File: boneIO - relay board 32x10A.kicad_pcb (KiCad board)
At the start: 2 copper layers, 197 x 102 mm, 116 parts, among them J1 Screw_Terminal_01x03, J10 Screw_Terminal_01x03, J11 Screw_Terminal_01x03, J12 Conn_02x04_Odd_Even, J13 Screw_Terminal_01x03, J14 Screw_Terminal_01x03, J15 Screw_Terminal_01x03, J16 Screw_Terminal_01x03, J17 Screw_Terminal_01x03, J2 Screw_Terminal_01x03, J3 Screw_Terminal_01x03, J4 Screw_Terminal_01x03, J5 Screw_Terminal_01x03, J6 Screw_Terminal_01x03, J7 Screw_Terminal_01x03, J8 Screw_Terminal_01x03, J9 Screw_Terminal_01x03, K1 HF32F/024-ZS3, K10 HF32F/024-ZS3, K11 HF32F/024-ZS3, K12 HF32F/024-ZS3, K13 HF32F/024-ZS3, K14 HF32F/024-ZS3, K15 HF32F/024-ZS3, K16 HF32F/024-ZS3, K17 HF32F/024-ZS3, K18 HF32F/024-ZS3, K19 HF32F/024-ZS3, K2 HF32F/024-ZS3, K20 HF32F/024-ZS3, K21 HF32F/024-ZS3, K22 HF32F/024-ZS3, K23 HF32F/024-ZS3, K24 HF32F/024-ZS3, K25 HF32F/024-ZS3, K26 HF32F/024-ZS3, K27 HF32F/024-ZS3, K28 HF32F/024-ZS3, K29 HF32F/024-ZS3, K3 HF32F/024-ZS3, K30 HF32F/024-ZS3, K31 HF32F/024-ZS3, K32 HF32F/024-ZS3, K4 HF32F/024-ZS3, K5 HF32F/024-ZS3, K6 HF32F/024-ZS3, K7 HF32F/024-ZS3, K8 HF32F/024-ZS3, K9 HF32F/024-ZS3, SW1 SW_DIP_x03, SW2 SW_DIP_x03, SW3 SW_DIP_x03, U1 PCF8575, U2 ULN2803A, U21 MCP9808_SO8, U22 LM75_MSOP, U3 ULN2803A, U4 PCF8575, U5 ULN2803A, U6 ULN2803A

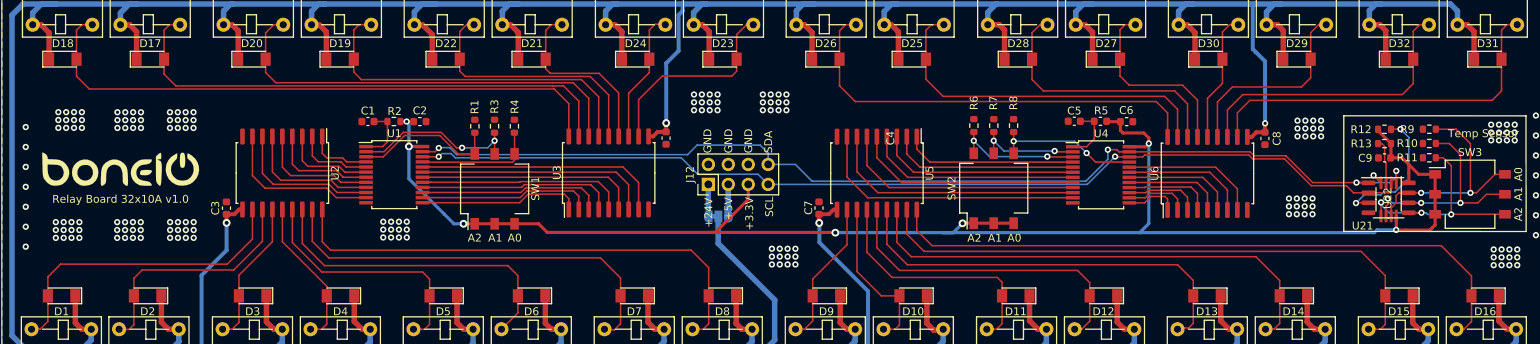
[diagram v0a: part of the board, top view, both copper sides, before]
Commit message: relay board 32x10A v0.1
Dodanie PCF8575
Dodanie MCP23017
Dodanie diody LL4148
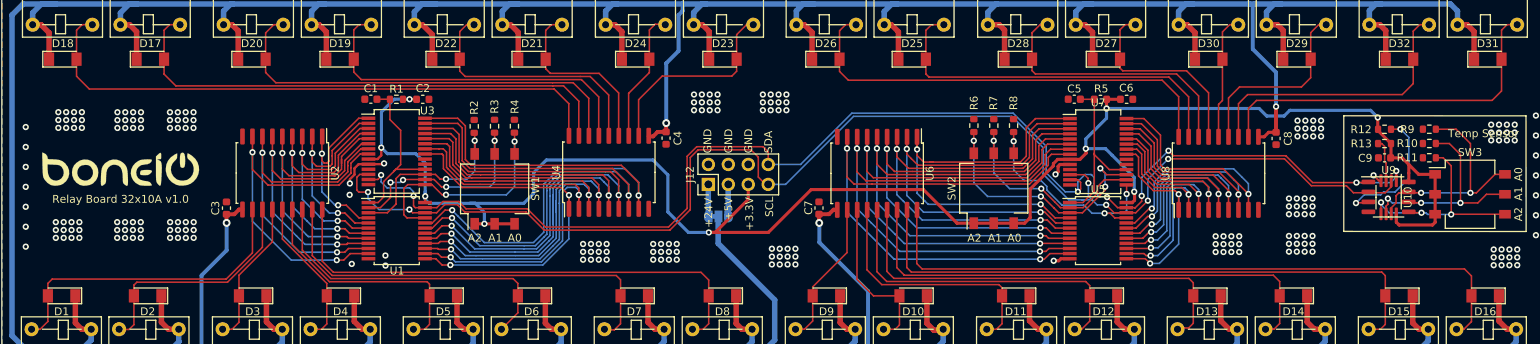
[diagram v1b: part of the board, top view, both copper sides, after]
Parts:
- removed U21: MCP9808_SO8, Package_SO:SO-8_3.9x4.9mm_P1.27mm
- removed U22: LM75_MSOP, Package_SO:MSOP-8_3x3mm_P0.65mm
- added U10: LM75_MSOP, Package_SO:MSOP-8_3x3mm_P0.65mm, F.Cu at (464.8, 314.4)
- added U7: MCP23017_SS, Package_SO:SSOP-28_5.3x10.2mm_P0.65mm, F.Cu at (427.8, 308.6)
- added U8: ULN2803A, Package_SO:SOIC-18W_7.5x11.6mm_P1.27mm, F.Cu at (443.1, 311.3)
- added U9: MCP9808_SO8, Package_SO:SO-8_3.9x4.9mm_P1.27mm, F.Cu at (464.8, 314.3)
- R1: value 10k -> 4.7k
- R2: value 4.7k -> 10k
- U3: value ULN2803A -> MCP23017_SS; footprint Package_SO:SOIC-18W_7.5x11.6mm_P1.27mm -> Package_SO:SSOP-28_5.3x10.2mm_P0.65mm
- U4: value PCF8575 -> ULN2803A; footprint Package_SO:SSOP-24_5.3x8.2mm_P0.65mm -> Package_SO:SOIC-18W_7.5x11.6mm_P1.27mm
- U5: value ULN2803A -> PCF8575; footprint Package_SO:SOIC-18W_7.5x11.6mm_P1.27mm -> Package_SO:SSOP-24_5.3x8.2mm_P0.65mm
- moved U4 62.7 mm to (365.5, 311.2), turned to 90 degrees
- moved U6 42.1 mm to (399.6, 311.3), turned to -90 degrees
- moved U5 29.1 mm to (427.8, 318.6), turned to 0 degrees
- moved U3 27.1 mm to (338.4, 308.5), turned to 0 degrees
- moved R1 10.6 mm to (338.4, 301.9), turned to 180 degrees
- moved R2 10.2 mm to (348.3, 305.3), turned to 90 degrees
- moved U1 7.14 mm to (338.4, 318.6)
- moved C2 2.86 mm to (341.8, 301.9)
- moved C1 2.86 mm to (335.2, 301.9)
- moved C6 2.85 mm to (431.4, 301.9)
- moved C5 2.81 mm to (424.8, 301.9)
- moved R5 2.80 mm to (428.1, 301.9)
- moved C8 1.42 mm to (450.5, 306.9)
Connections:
- C1 pad 1: Net-(C1-Pad1) -> INT_01
- C5 pad 1: Net-(C5-Pad1) -> INT_02
- R1 pad 1: Net-(R1-Pad1) -> +3V3
- R1 pad 2: GND -> INT_01
- R2 pad 1: +3V3 -> A2_1
- R2 pad 2: Net-(C1-Pad1) -> GND
- R3 pad 1: Net-(R3-Pad1) -> A1_1
- R4 pad 1: Net-(R4-Pad1) -> A0_1
- R5 pad 2: Net-(C5-Pad1) -> INT_02
- R6 pad 1: Net-(R6-Pad1) -> A2_2
- R7 pad 1: Net-(R7-Pad1) -> A1_2
- R8 pad 1: Net-(R8-Pad1) -> A0_2
- SW1 pad 4: Net-(R4-Pad1) -> A0_1
- SW1 pad 5: Net-(R3-Pad1) -> A1_1
- SW1 pad 6: Net-(R1-Pad1) -> A2_1
- SW2 pad 4: Net-(R8-Pad1) -> A0_2
- SW2 pad 5: Net-(R7-Pad1) -> A1_2
- SW2 pad 6: Net-(R6-Pad1) -> A2_2
- U1 pad 1: Net-(C1-Pad1) -> INT_01
- U1 pad 10: Net-(U1-Pad10) -> P6_1
- U1 pad 11: Net-(U1-Pad11) -> P7_1
- U1 pad 13: Net-(U1-Pad13) -> P8_1
- U1 pad 14: Net-(U1-Pad14) -> P9_1
- U1 pad 15: Net-(U1-Pad15) -> P10_1
- U1 pad 16: Net-(U1-Pad16) -> P11_1
- U1 pad 17: Net-(U1-Pad17) -> P12_1
- U1 pad 18: Net-(U1-Pad18) -> P13_1
- U1 pad 19: Net-(U1-Pad19) -> P14_1
- U1 pad 2: Net-(R3-Pad1) -> A1_1
- U1 pad 20: Net-(U1-Pad20) -> P15_1
- U1 pad 21: Net-(R4-Pad1) -> A0_1
- U1 pad 3: Net-(R1-Pad1) -> A2_1
- U1 pad 4: Net-(U1-Pad4) -> P0_1
- U1 pad 5: Net-(U1-Pad5) -> P1_1
- U1 pad 6: Net-(U1-Pad6) -> P2_1
- U1 pad 7: Net-(U1-Pad7) -> P3_1
- U1 pad 8: Net-(U1-Pad8) -> P4_1
- U1 pad 9: Net-(U1-Pad9) -> P5_1
- U2 pad 1: Net-(U1-Pad4) -> P0_1
- U2 pad 2: Net-(U1-Pad5) -> P1_1
- U2 pad 3: Net-(U1-Pad6) -> P2_1
- U2 pad 4: Net-(U1-Pad7) -> P3_1
- U2 pad 5: Net-(U1-Pad8) -> P4_1
- U2 pad 6: Net-(U1-Pad9) -> P5_1
- U2 pad 7: Net-(U1-Pad10) -> P6_1
- U2 pad 8: Net-(U1-Pad11) -> P7_1
- U3 pad 1: Net-(U1-Pad13) -> P0_1
- U3 pad 10: VCC -> GND
- U3 pad 11: RELAY23 -> unconnected-(U3-Pad11)
- U3 pad 12: RELAY24 -> SCL
- U3 pad 13: RELAY21 -> SDA
- U3 pad 14: RELAY22 -> unconnected-(U3-Pad14)
- U3 pad 15: RELAY19 -> A0_1
- U3 pad 16: RELAY20 -> A1_1
- U3 pad 17: RELAY17 -> A2_1
- U3 pad 18: RELAY18 -> INT_01
- U3 pad 2: Net-(U1-Pad14) -> P1_1
- U3 pad 3: Net-(U1-Pad15) -> P2_1
- U3 pad 4: Net-(U1-Pad16) -> P3_1
- U3 pad 5: Net-(U1-Pad17) -> P4_1
- U3 pad 6: Net-(U1-Pad18) -> P5_1
- U3 pad 7: Net-(U1-Pad19) -> P6_1
- U3 pad 8: Net-(U1-Pad20) -> P7_1
- U3 pad 9: GND -> +3V3
- U4 pad 1: Net-(C5-Pad1) -> P8_1
- U4 pad 10: Net-(U4-Pad10) -> VCC
- U4 pad 11: Net-(U4-Pad11) -> RELAY23
- U4 pad 12: GND -> RELAY24
- U4 pad 13: Net-(U4-Pad13) -> RELAY21
- U4 pad 14: Net-(U4-Pad14) -> RELAY22
- U4 pad 15: Net-(U4-Pad15) -> RELAY19
- U4 pad 16: Net-(U4-Pad16) -> RELAY20
- U4 pad 17: Net-(U4-Pad17) -> RELAY17
- U4 pad 18: Net-(U4-Pad18) -> RELAY18
- U4 pad 2: Net-(R7-Pad1) -> P9_1
- U4 pad 3: Net-(R6-Pad1) -> P10_1
- U4 pad 4: Net-(U4-Pad4) -> P11_1
- U4 pad 5: Net-(U4-Pad5) -> P12_1
- U4 pad 6: Net-(U4-Pad6) -> P13_1
- U4 pad 7: Net-(U4-Pad7) -> P14_1
- U4 pad 8: Net-(U4-Pad8) -> P15_1
- U4 pad 9: Net-(U4-Pad9) -> GND
- U5 pad 1: Net-(U4-Pad4) -> INT_02
- U5 pad 10: VCC -> P6_2
- U5 pad 11: RELAY9 -> P7_2
- U5 pad 12: RELAY10 -> GND
- U5 pad 13: RELAY11 -> P8_2
- U5 pad 14: RELAY12 -> P9_2
- U5 pad 15: RELAY13 -> P10_2
- U5 pad 16: RELAY14 -> P11_2
- U5 pad 17: RELAY15 -> P12_2
- U5 pad 18: RELAY16 -> P13_2
- U5 pad 2: Net-(U4-Pad5) -> A1_2
- U5 pad 3: Net-(U4-Pad6) -> A2_2
- U5 pad 4: Net-(U4-Pad7) -> P0_2
- U5 pad 5: Net-(U4-Pad8) -> P1_2
- U5 pad 6: Net-(U4-Pad9) -> P2_2
- U5 pad 7: Net-(U4-Pad10) -> P3_2
- U5 pad 8: Net-(U4-Pad11) -> P4_2
- U5 pad 9: GND -> P5_2
- U6 pad 1: Net-(U4-Pad13) -> P0_2
- U6 pad 11: RELAY31 -> RELAY9
- U6 pad 12: RELAY32 -> RELAY10
- U6 pad 13: RELAY29 -> RELAY11
- U6 pad 14: RELAY30 -> RELAY12
- U6 pad 15: RELAY27 -> RELAY13
- U6 pad 16: RELAY28 -> RELAY14
- U6 pad 17: RELAY25 -> RELAY15
- U6 pad 18: RELAY26 -> RELAY16
- U6 pad 2: Net-(U4-Pad14) -> P1_2
- U6 pad 3: Net-(U4-Pad15) -> P2_2
- U6 pad 4: Net-(U4-Pad16) -> P3_2
- U6 pad 5: Net-(U4-Pad17) -> P4_2
- U6 pad 6: Net-(U4-Pad18) -> P5_2
- U6 pad 7: Net-(U4-Pad19) -> P6_2
- U6 pad 8: Net-(U4-Pad20) -> P7_2
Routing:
- net P15_1: track 0.00 -> 76.1 mm, vias 0 -> 2
- net P7_2: track 0.00 -> 75.3 mm, vias 0 -> 2
- net P14_1: track 0.00 -> 72.4 mm, vias 0 -> 2
- net P6_2: track 0.00 -> 71.6 mm, vias 0 -> 2
- net P12_1: track 0.00 -> 68.8 mm, vias 0 -> 2
- net P13_1: track 0.00 -> 68.8 mm, vias 0 -> 2
- net P5_2: track 0.00 -> 68.5 mm, vias 0 -> 2
- net P4_2: track 0.00 -> 65.1 mm, vias 0 -> 2
- net P11_1: track 0.00 -> 63.1 mm, vias 0 -> 2
- net P3_2: track 0.00 -> 62.1 mm, vias 0 -> 2
- net P2_2: track 0.00 -> 58.7 mm, vias 0 -> 2
- net P10_1: track 0.00 -> 57.5 mm, vias 0 -> 2
- net P1_2: track 0.00 -> 55.9 mm, vias 0 -> 2
- net P0_2: track 0.00 -> 55.0 mm, vias 0 -> 2
- net P9_1: track 0.00 -> 54.2 mm, vias 0 -> 2
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
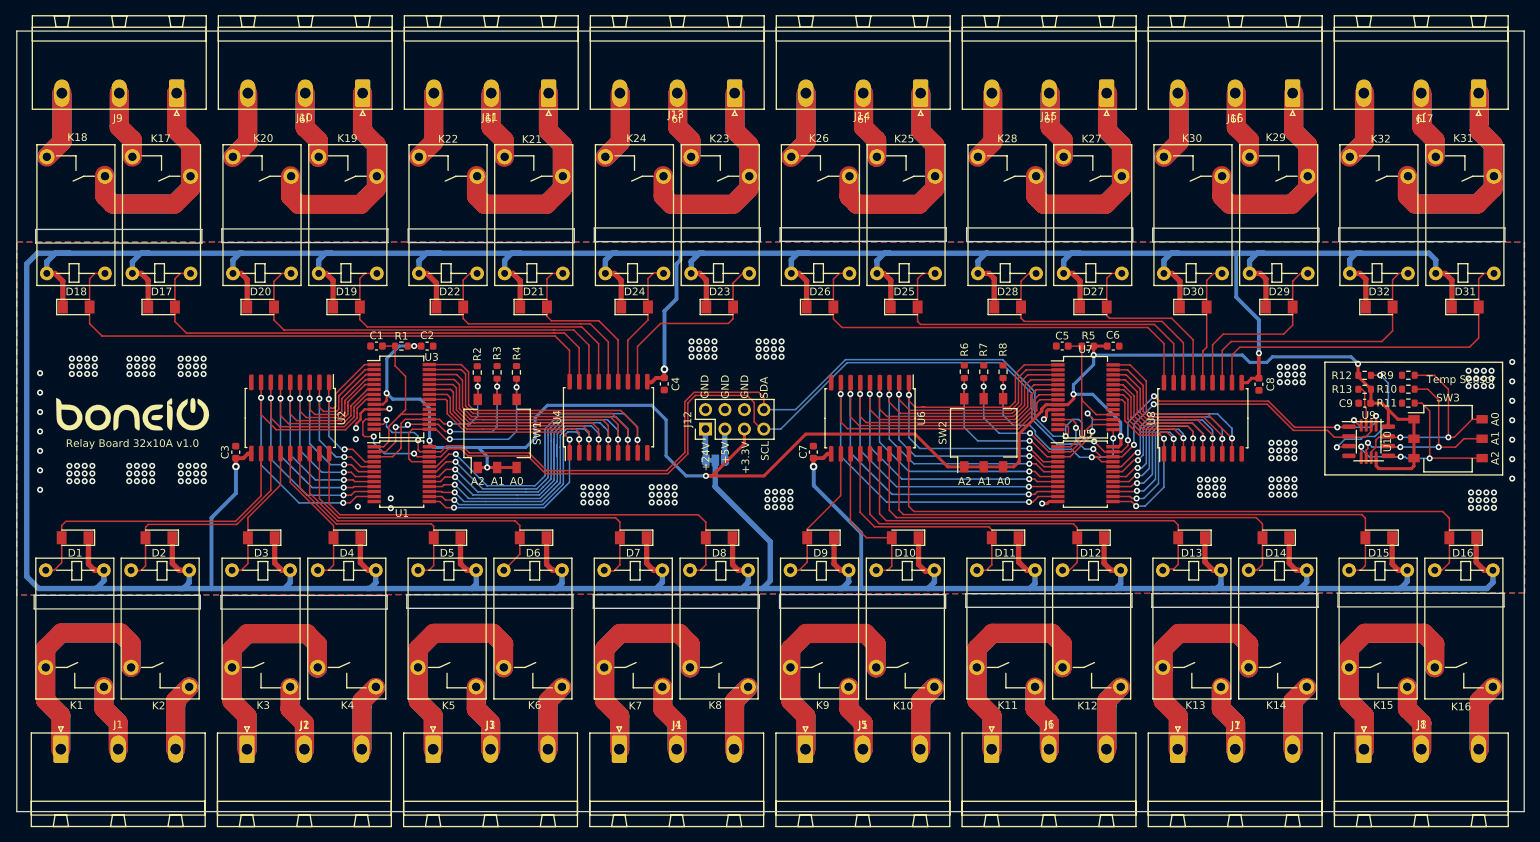
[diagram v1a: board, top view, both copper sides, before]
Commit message: relay board 32x10A v0.1 (rev2)
rozdzielenie GND
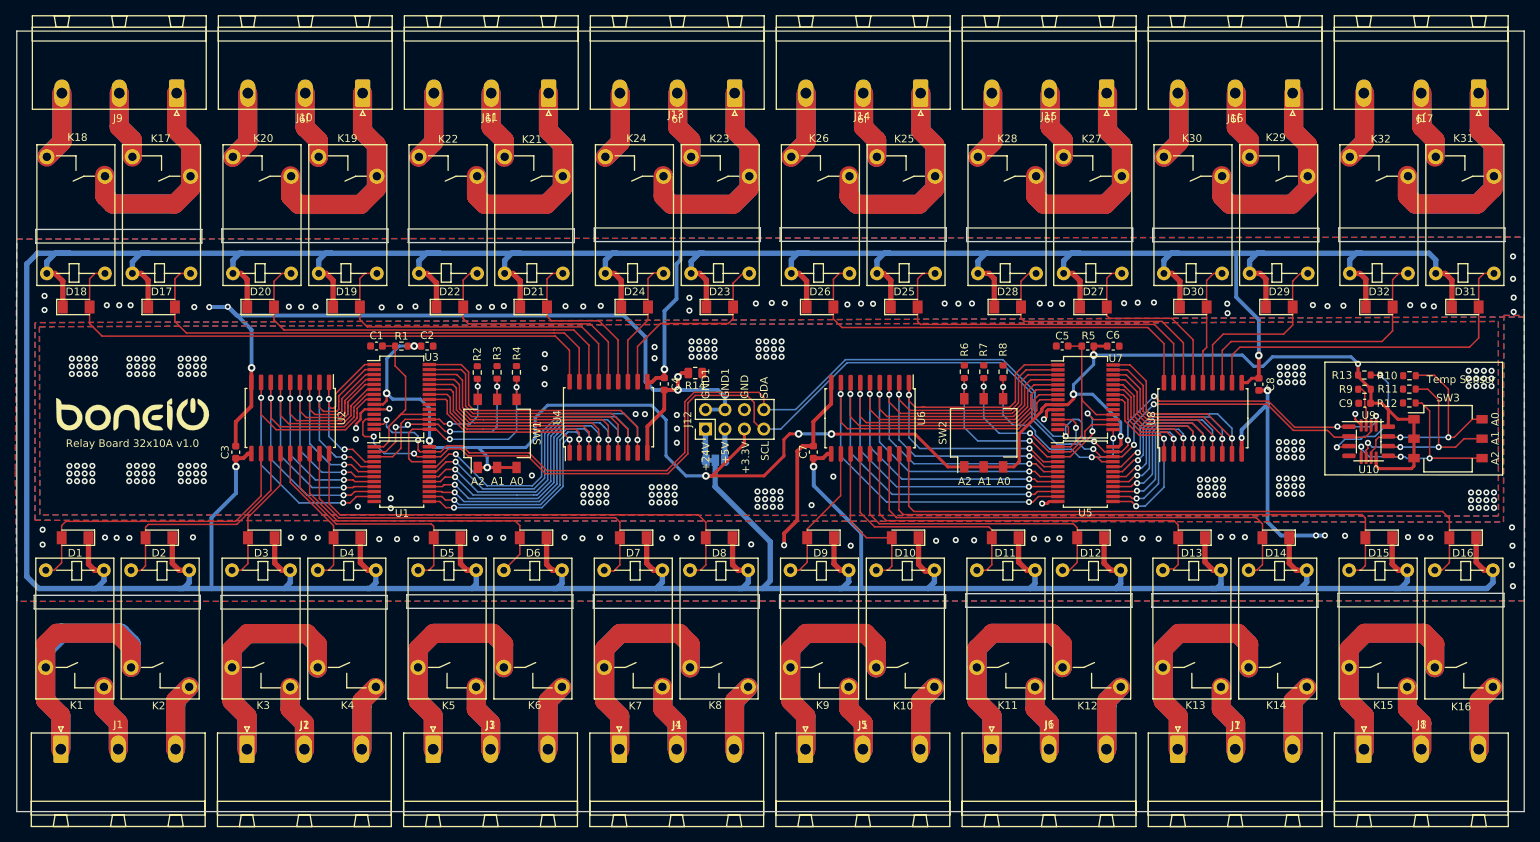
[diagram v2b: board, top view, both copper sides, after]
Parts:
- added R14: 0k, Resistor_SMD:R_0805_2012Metric, F.Cu at (376.8, 305.4)
- R12: value 4.7k -> 10k
- R9: value 10k -> 4.7k
- moved R12 6.86 mm to (470.1, 309.3), turned to 180 degrees
- moved R9 6.02 mm to (464.3, 307.5)
- moved R13 1.86 mm to (464.3, 305.7), turned to 0 degrees
- moved R11 1.83 mm to (470.1, 307.5)
- moved R10 1.77 mm to (470.1, 305.7)
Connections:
- C3 pad 1: GND -> GND1
- C4 pad 1: GND -> GND1
- C7 pad 1: GND -> GND1
- C8 pad 1: GND -> GND1
- J12 pad 2: GND -> GND1
- J12 pad 4: GND -> GND1
- R12 pad 1: +3V3 -> Net-(R12-Pad1)
- R12 pad 2: Net-(R12-Pad2) -> GND
- R9 pad 1: Net-(R9-Pad1) -> +3V3
- R9 pad 2: GND -> Net-(R9-Pad2)
- SW3 pad 4: Net-(R11-Pad1) -> Net-(R12-Pad1)
- SW3 pad 5: Net-(R10-Pad1) -> Net-(R11-Pad1)
- SW3 pad 6: Net-(R9-Pad1) -> Net-(R10-Pad1)
- U10 pad 3: Net-(R13-Pad2) -> Net-(R9-Pad2)
- U10 pad 5: Net-(R11-Pad1) -> Net-(R12-Pad1)
- U10 pad 6: Net-(R10-Pad1) -> Net-(R11-Pad1)
- U10 pad 7: Net-(R9-Pad1) -> Net-(R10-Pad1)
- U2 pad 9: GND -> GND1
- U4 pad 9: GND -> GND1
- U6 pad 9: GND -> GND1
- U8 pad 9: GND -> GND1
- U9 pad 3: Net-(R12-Pad2) -> Net-(R13-Pad2)
- U9 pad 5: Net-(R11-Pad1) -> Net-(R12-Pad1)
- U9 pad 6: Net-(R10-Pad1) -> Net-(R11-Pad1)
- U9 pad 7: Net-(R9-Pad1) -> Net-(R10-Pad1)
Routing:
- net GND1: track 0.00 -> 173.6 mm, vias 0 -> 100
- net Net-(R9-Pad1): track 29.3 -> 0.00 mm, vias 2 -> 0
- net Net-(R12-Pad1): track 0.00 -> 28.6 mm, vias 0 -> 3
- net Net-(R12-Pad2): track 17.6 -> 0.00 mm, vias 2 -> 0
- net Net-(R13-Pad2): track 5.70 -> 17.6 mm, vias 0 -> 2
- net Net-(R9-Pad2): track 0.00 -> 5.70 mm
- net P12_1: track 68.8 -> 65.4 mm
- net +3V3: track 232.8 -> 234.5 mm, vias 9 -> 11
- net P11_1: track 63.1 -> 61.7 mm
- net Net-(R11-Pad1): track 28.6 -> 29.4 mm
- net GND: track 12.3 -> 12.9 mm, vias 227 -> 226
- net Net-(R10-Pad1): track 29.4 -> 29.3 mm, vias 3 -> 2
- added copper zone on B.Cu, net GND1
- added copper zone on F.Cu, net GND1
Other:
- board text added: "GND1"

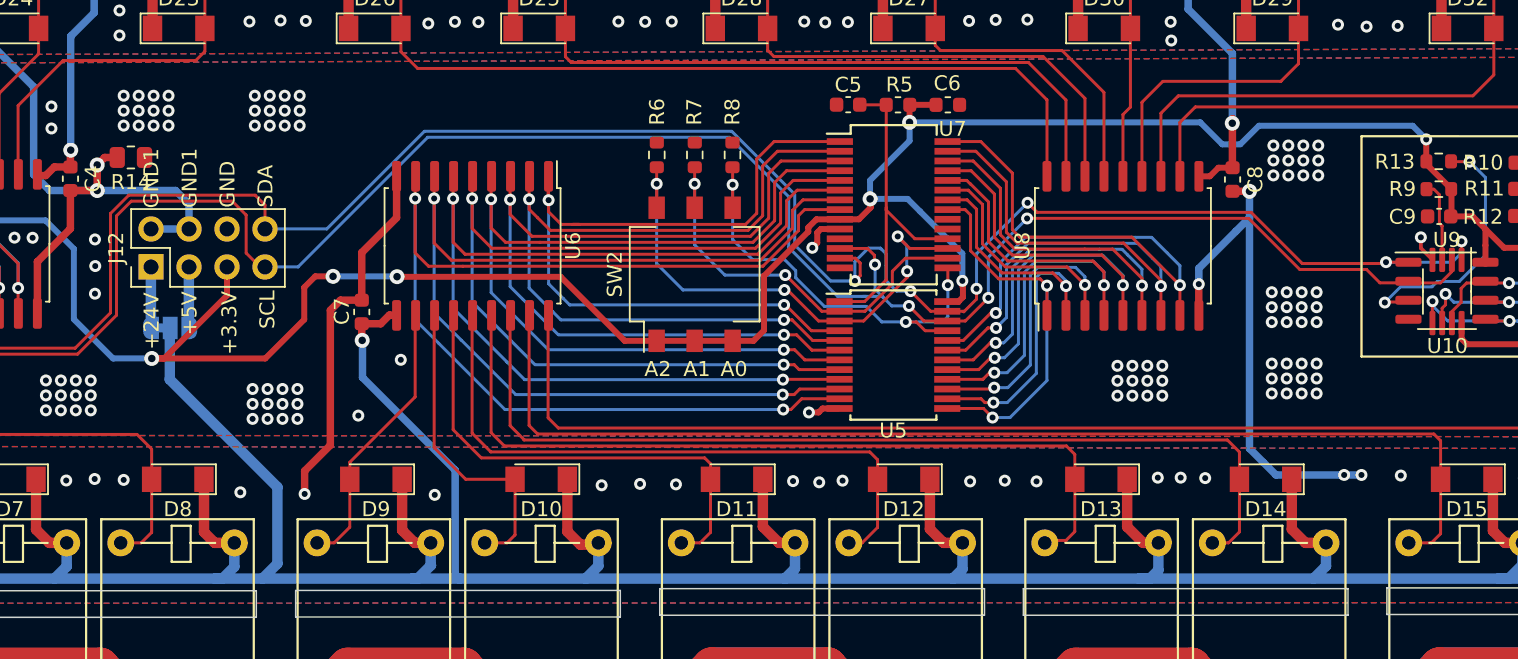
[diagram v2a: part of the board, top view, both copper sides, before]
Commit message: v0.1
dodanie dławika filtrujacego
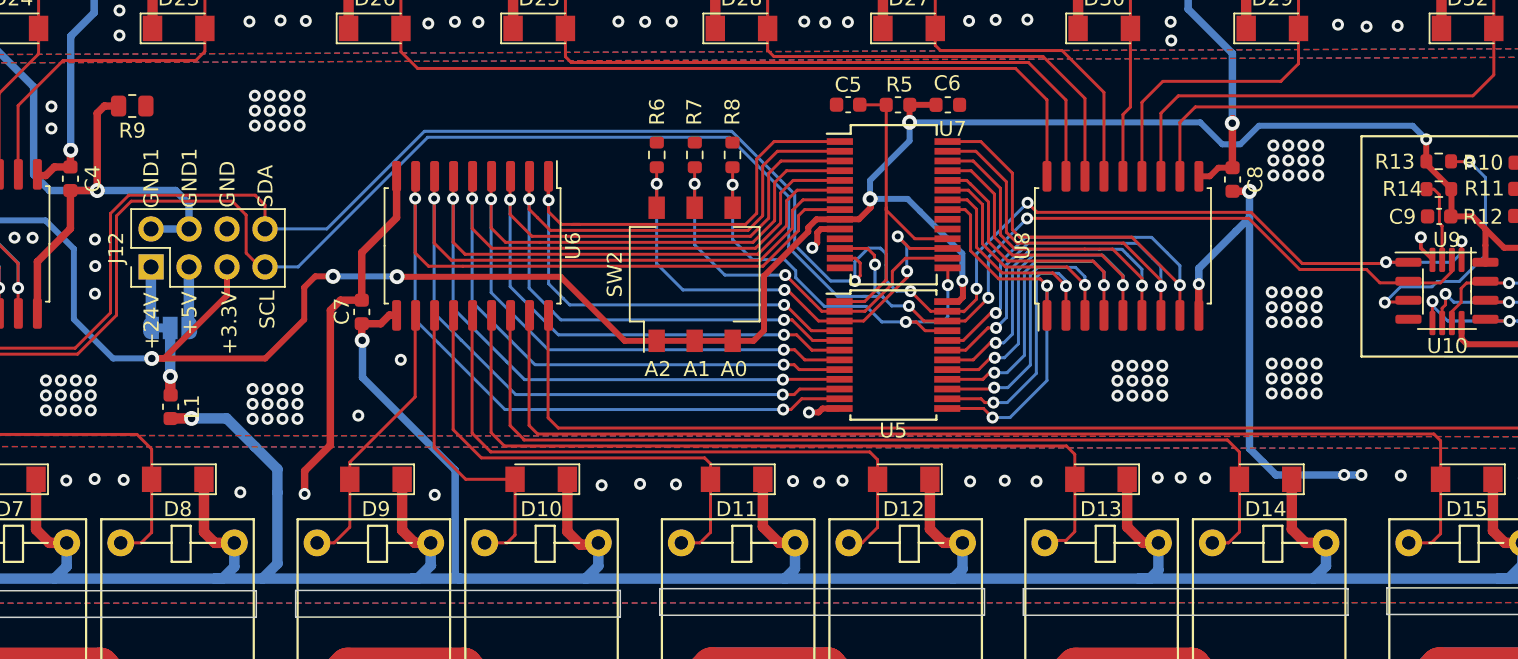
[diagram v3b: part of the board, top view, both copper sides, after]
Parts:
- added L1: LQG18HN10NJ00D, Inductor_SMD:L_0603_1608Metric, F.Cu at (379.5, 322.1)
- moved R9 3.44 mm to (376.9, 302.0)
- renumbered R9 to R14, R14 to R9
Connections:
- JP1 pad 2: VCC -> Net-(JP1-Pad2)
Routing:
- net Net-(JP1-Pad2): track 0.00 -> 4.49 mm, vias 0 -> 1
- net VCC: track 816.3 -> 812.6 mm, vias 4 -> 5
- net GND1: track 173.6 -> 177.2 mm, vias 100 -> 99
- net GND: vias 226 -> 214
